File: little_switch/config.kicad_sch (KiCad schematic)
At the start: 58 parts, among them J7 Conn_02x11_Odd_Even, J8 Conn_01x02, SW1 SW_Push, U1 KSZ8567S, U2 DS90LT012AQMFE/NOPB, Y1 25 MHz

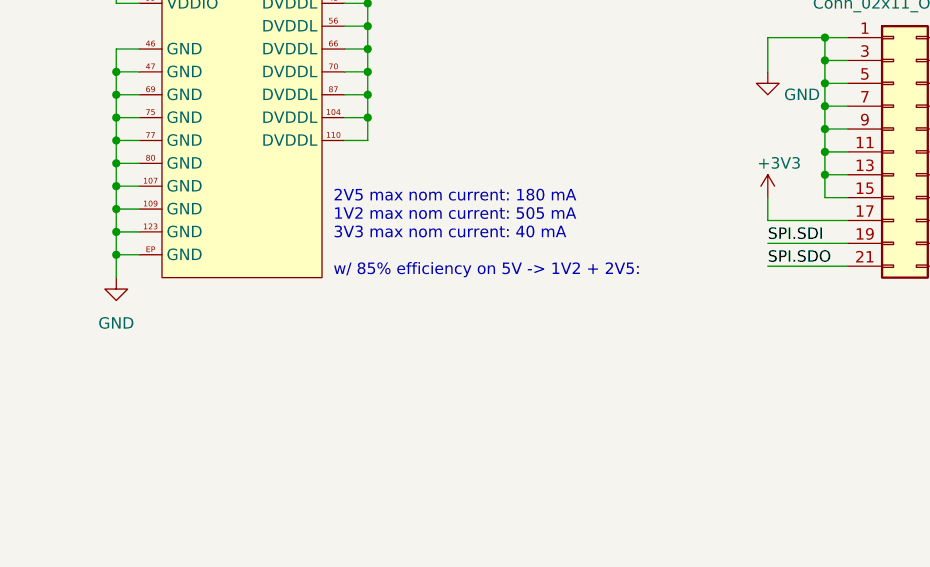
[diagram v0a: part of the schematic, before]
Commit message: adding housekeeping board
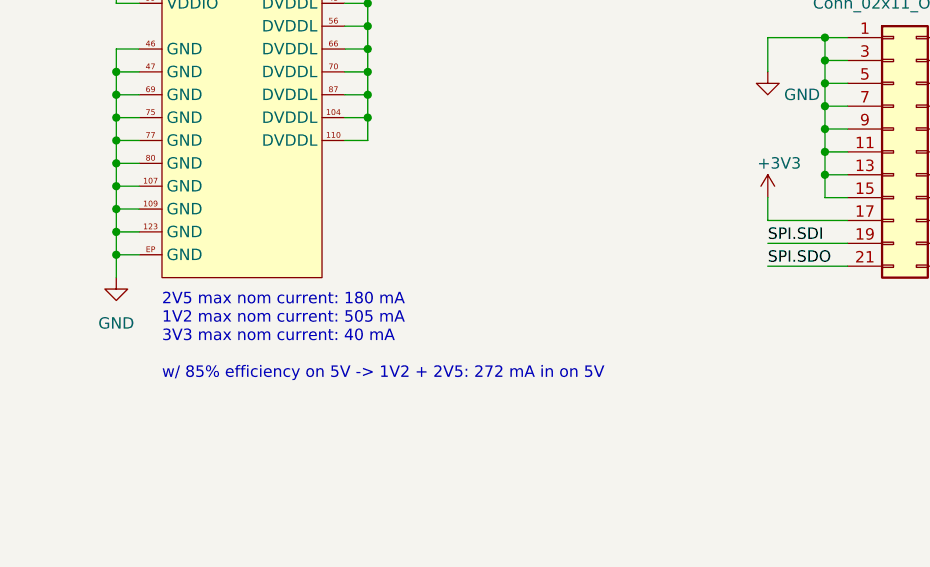
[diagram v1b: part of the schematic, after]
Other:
- note added: "2V5 max nom current: 180 mA 1V2 max nom current: 505 mA 3V3 max nom current: 40 mA w/ 85% efficiency on 5V -> 1V2 + 2V5: 272 mA in on 5V"
- note removed: "2V5 max nom current: 180 mA 1V2 max nom current: 505 mA 3V3 max nom current: 40 mA w/ 85% efficiency on 5V -> 1V2 + 2V5:"
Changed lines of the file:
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@@
     (effects (font (size 1.27 1.27)) (justify right bottom))
   )
-  (text "2V5 max nom current: 180 mA\n1V2 max nom current: 505 mA\n3V3 max nom current: 40 mA\n\nw/ 85% efficiency on 5V -> 1V2 + 2V5:\n"
-    (at 63.5 93.98 0)
+  (text "2V5 max nom current: 180 mA\n1V2 max nom current: 505 mA\n3V3 max nom current: 40 mA\n\nw/ 85% efficiency on 5V -> 1V2 + 2V5: 272 mA in on 5V\n"
+    (at 44.45 105.41 0)
     (effects (font (size 1.27 1.27)) (justify left bottom))
   )
